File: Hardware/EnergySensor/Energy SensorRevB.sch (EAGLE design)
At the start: 42 parts, among them IC2 ATMega328p-pu, IC3 ld33v, Q1 16MHz, X1 MAINS IN

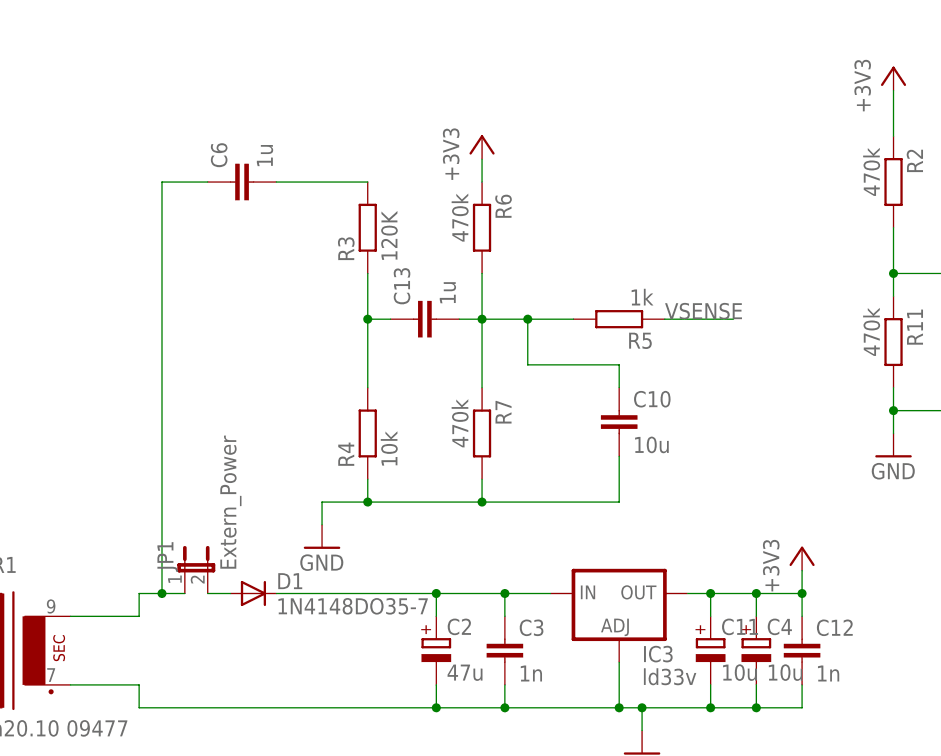
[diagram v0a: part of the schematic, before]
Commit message: FIXED MAJOR BUG  - schematic was incorrect for power measurements
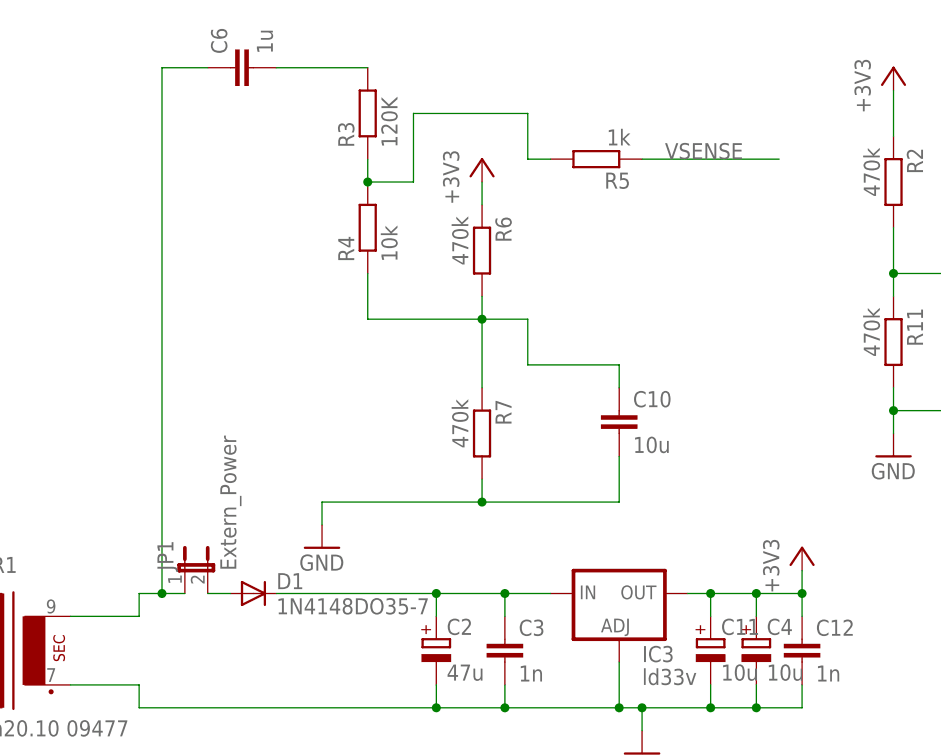
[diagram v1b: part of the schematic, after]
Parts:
- removed C13: 1u, rcl:C-EUC1206K
- R4: device rcl:R-EU_0207/7 -> rcl:R-EU_R1206
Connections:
- removed net N$10: C10.1, C13.2, R5.2, R6.2, R7.1
- new net N$11: C10.1, R4.1, R6.2, R7.1
- net GND: no longer R4.1
- net N$9: now also R5.2; no longer C13.1
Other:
- moved on the sheet: C6, R3, R4, R5, R6
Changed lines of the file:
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@@
 <part name="C6" library="rcl" deviceset="C-EU" device="C1206K" value="1u"/>
 <part name="R3" library="rcl" deviceset="R-EU_" device="0207/7" value="120K"/>
-<part name="R4" library="rcl" deviceset="R-EU_" device="0207/7" value="10k"/>
+<part name="R4" library="rcl" deviceset="R-EU_" device="R1206" value="10k"/>
 <part name="R5" library="rcl" deviceset="R-EU_" device="0207/7" value="1k"/>
 <part name="R6" library="rcl" deviceset="R-EU_" device="0207/7" value="470k"/>
@@
 <part name="GND9" library="supply1" deviceset="GND" device=""/>
 <part name="+3V6" library="supply1" deviceset="+3V3" device=""/>
-<part name="C13" library="rcl" deviceset="C-EU" device="C1206K" value="1u"/>
 <part name="JP1" library="jumper" deviceset="JP1E" device="" value="Extern_Power"/>
 <part name="H1" library="holes" deviceset="MOUNT-HOLE" device="2.8"/>
@@
 <instance part="C3" gate="G$1" x="101.6" y="78.74"/>
 <instance part="GND1" gate="1" x="116.84" y="66.04"/>
-<instance part="C6" gate="G$1" x="71.12" y="129.54" rot="R90"/>
-<instance part="R3" gate="G$1" x="86.36" y="124.46" rot="R90"/>
-<instance part="R4" gate="G$1" x="86.36" y="101.6" rot="R90"/>
-<instance part="R5" gate="G$1" x="114.3" y="114.3" rot="R180"/>
-<instance part="R6" gate="G$1" x="99.06" y="124.46" rot="R270"/>
+<instance part="C6" gate="G$1" x="71.12" y="142.24" rot="R90"/>
+<instance part="R3" gate="G$1" x="86.36" y="137.16" rot="R90"/>
+<instance part="R4" gate="G$1" x="86.36" y="124.46" rot="R90"/>
+<instance part="R5" gate="G$1" x="111.76" y="132.08" rot="R180"/>
+<instance part="R6" gate="G$1" x="99.06" y="121.92" rot="R270"/>
 <instance part="R7" gate="G$1" x="99.06" y="101.6" rot="R270"/>
 <instance part="GND3" gate="1" x="81.28" y="88.9"/>
@@
 <instance part="R10" gate="G$1" x="175.26" y="48.26" rot="R90"/>
 <instance part="GND9" gate="1" x="180.34" y="25.4"/>
-<instance part="+3V6" gate="G$1" x="99.06" y="134.62"/>
-<instance part="C13" gate="G$1" x="91.44" y="114.3" rot="R90"/>
+<instance part="+3V6" gate="G$1" x="99.06" y="132.08"/>
 <instance part="JP1" gate="A" x="66.04" y="86.36"/>
 <instance part="H1" gate="G$1" x="241.3" y="40.64"/>
@@
 <wire x1="60.96" y1="83.82" x2="63.5" y2="83.82" width="0.1524" layer="91"/>
 <pinref part="C6" gate="G$1" pin="1"/>
-<wire x1="63.5" y1="83.82" x2="63.5" y2="129.54" width="0.1524" layer="91"/>
-<wire x1="63.5" y1="129.54" x2="68.58" y2="129.54" width="0.1524" layer="91"/>
+<wire x1="63.5" y1="83.82" x2="63.5" y2="142.24" width="0.1524" layer="91"/>
+<wire x1="63.5" y1="142.24" x2="68.58" y2="142.24" width="0.1524" layer="91"/>
 <pinref part="TR1" gate="1" pin="S4"/>
 <wire x1="60.96" y1="81.28" x2="53.34" y2="81.28" width="0.1524" layer="91"/>
@@
 <pinref part="R7" gate="G$1" pin="2"/>
 <wire x1="99.06" y1="96.52" x2="99.06" y2="93.98" width="0.1524" layer="91"/>
-<wire x1="99.06" y1="93.98" x2="86.36" y2="93.98" width="0.1524" layer="91"/>
+<wire x1="99.06" y1="93.98" x2="81.28" y2="93.98" width="0.1524" layer="91"/>
 <pinref part="GND3" gate="1" pin="GND"/>
-<wire x1="86.36" y1="93.98" x2="81.28" y2="93.98" width="0.1524" layer="91"/>
 <wire x1="81.28" y1="93.98" x2="81.28" y2="91.44" width="0.1524" layer="91"/>
 <pinref part="C10" gate="G$1" pin="2"/>
@@
 <wire x1="114.3" y1="93.98" x2="99.06" y2="93.98" width="0.1524" layer="91"/>
 <junction x="99.06" y="93.98"/>
-<pinref part="R4" gate="G$1" pin="1"/>
-<wire x1="86.36" y1="96.52" x2="86.36" y2="93.98" width="0.1524" layer="91"/>
-<junction x="86.36" y="93.98"/>
 </segment>
 <segment>
@@
 <pinref part="C6" gate="G$1" pin="2"/>
 <pinref part="R3" gate="G$1" pin="2"/>
-<wire x1="76.2" y1="129.54" x2="86.36" y2="129.54" width="0.1524" layer="91"/>
+<wire x1="76.2" y1="142.24" x2="86.36" y2="142.24" width="0.1524" layer="91"/>
 </segment>
 </net>
@@
 <pinref part="R3" gate="G$1" pin="1"/>
 <pinref part="R4" gate="G$1" pin="2"/>
-<wire x1="86.36" y1="119.38" x2="86.36" y2="114.3" width="0.1524" layer="91"/>
-<junction x="86.36" y="114.3"/>
-<wire x1="86.36" y1="114.3" x2="86.36" y2="106.68" width="0.1524" layer="91"/>
-<pinref part="C13" gate="G$1" pin="1"/>
-<wire x1="88.9" y1="114.3" x2="86.36" y2="114.3" width="0.1524" layer="91"/>
+<wire x1="86.36" y1="132.08" x2="86.36" y2="129.54" width="0.1524" layer="91"/>
+<pinref part="R5" gate="G$1" pin="2"/>
+<wire x1="106.68" y1="132.08" x2="104.14" y2="132.08" width="0.1524" layer="91"/>
+<wire x1="104.14" y1="132.08" x2="104.14" y2="137.16" width="0.1524" layer="91"/>
+<wire x1="104.14" y1="137.16" x2="91.44" y2="137.16" width="0.1524" layer="91"/>
+<wire x1="91.44" y1="137.16" x2="91.44" y2="129.54" width="0.1524" layer="91"/>
+<wire x1="91.44" y1="129.54" x2="86.36" y2="129.54" width="0.1524" layer="91"/>
+<junction x="86.36" y="129.54"/>
 </segment>
 </net>
@@
 <segment>
 <pinref part="R5" gate="G$1" pin="1"/>
-<label x="119.38" y="114.3" size="1.778" layer="95"/>
-<wire x1="119.38" y1="114.3" x2="127" y2="114.3" width="0.1524" layer="91"/>
+<label x="119.38" y="132.08" size="1.778" layer="95"/>
+<wire x1="116.84" y1="132.08" x2="132.08" y2="132.08" width="0.1524" layer="91"/>
 </segment>
 <segment>
@@
 <segment>
 <pinref part="R6" gate="G$1" pin="1"/>
-<wire x1="99.06" y1="132.08" x2="99.06" y2="129.54" width="0.1524" layer="91"/>
+<wire x1="99.06" y1="129.54" x2="99.06" y2="127" width="0.1524" layer="91"/>
 <pinref part="+3V6" gate="G$1" pin="+3V3"/>
 </segment>
@@
 <pinref part="R10" gate="G$1" pin="2"/>
 <wire x1="175.26" y1="60.96" x2="175.26" y2="53.34" width="0.1524" layer="91"/>
-</segment>
-</net>
-<net name="N$10" class="0">
-<segment>
-<pinref part="R6" gate="G$1" pin="2"/>
-<pinref part="C13" gate="G$1" pin="2"/>
-<wire x1="99.06" y1="119.38" x2="99.06" y2="114.3" width="0.1524" layer="91"/>
-<wire x1="99.06" y1="114.3" x2="96.52" y2="114.3" width="0.1524" layer="91"/>
-<pinref part="R7" gate="G$1" pin="1"/>
-<wire x1="99.06" y1="106.68" x2="99.06" y2="114.3" width="0.1524" layer="91"/>
-<junction x="99.06" y="114.3"/>
-<pinref part="R5" gate="G$1" pin="2"/>
-<wire x1="109.22" y1="114.3" x2="104.14" y2="114.3" width="0.1524" layer="91"/>
-<pinref part="C10" gate="G$1" pin="1"/>
-<wire x1="104.14" y1="114.3" x2="99.06" y2="114.3" width="0.1524" layer="91"/>
-<wire x1="114.3" y1="106.68" x2="114.3" y2="109.22" width="0.1524" layer="91"/>
-<wire x1="114.3" y1="109.22" x2="104.14" y2="109.22" width="0.1524" layer="91"/>
-<wire x1="104.14" y1="109.22" x2="104.14" y2="114.3" width="0.1524" layer="91"/>
-<junction x="104.14" y="114.3"/>
 </segment>
 </net>
@@
 </segment>
 </net>
+<net name="N$11" class="0">
+<segment>
+<pinref part="R4" gate="G$1" pin="1"/>
+<wire x1="86.36" y1="119.38" x2="86.36" y2="114.3" width="0.1524" layer="91"/>
+<pinref part="R6" gate="G$1" pin="2"/>
+<wire x1="99.06" y1="116.84" x2="99.06" y2="114.3" width="0.1524" layer="91"/>
+<pinref part="R7" gate="G$1" pin="1"/>
+<wire x1="99.06" y1="106.68" x2="99.06" y2="114.3" width="0.1524" layer="91"/>
+<junction x="99.06" y="114.3"/>
+<pinref part="C10" gate="G$1" pin="1"/>
+<wire x1="104.14" y1="114.3" x2="99.06" y2="114.3" width="0.1524" layer="91"/>
+<wire x1="114.3" y1="106.68" x2="114.3" y2="109.22" width="0.1524" layer="91"/>
+<wire x1="114.3" y1="109.22" x2="104.14" y2="109.22" width="0.1524" layer="91"/>
+<wire x1="104.14" y1="109.22" x2="104.14" y2="114.3" width="0.1524" layer="91"/>
+<wire x1="86.36" y1="114.3" x2="99.06" y2="114.3" width="0.1524" layer="91"/>
+</segment>
+</net>

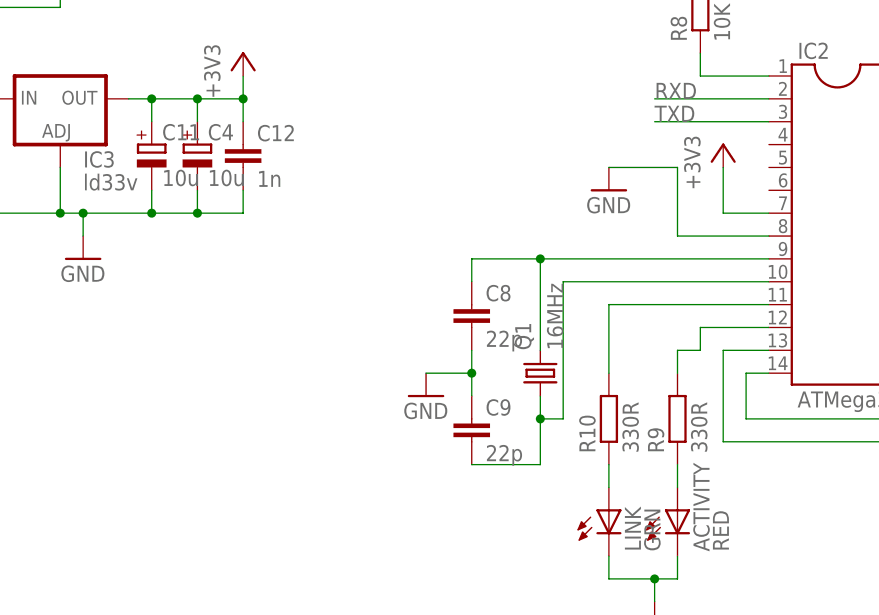
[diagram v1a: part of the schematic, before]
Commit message: updated BOM with finalised pricelist
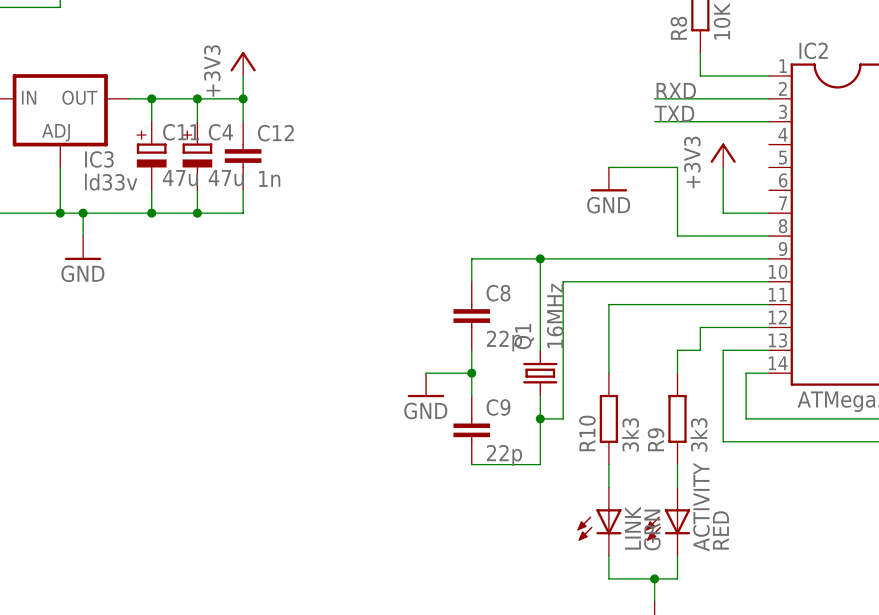
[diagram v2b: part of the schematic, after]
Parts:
- C11, C4: value 10u -> 47u
- R10, R9: value 330R -> 3k3
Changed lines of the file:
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@@
 <part name="+3V4" library="supply1" deviceset="+3V3" device=""/>
 <part name="+3V5" library="supply1" deviceset="+3V3" device=""/>
-<part name="C11" library="rcl" deviceset="CPOL-EU" device="E3.5-8" value="10u"/>
+<part name="C11" library="rcl" deviceset="CPOL-EU" device="E3.5-8" value="47u"/>
 <part name="C12" library="rcl" deviceset="C-EU" device="025-025X050" value="1n"/>
 <part name="LINK" library="led" deviceset="LED" device="5MM" value="GRN"/>
 <part name="ACTIVITY" library="led" deviceset="LED" device="5MM" value="RED"/>
-<part name="R9" library="rcl" deviceset="R-EU_" device="0207/7" value="330R"/>
-<part name="R10" library="rcl" deviceset="R-EU_" device="0207/7" value="330R"/>
+<part name="R9" library="rcl" deviceset="R-EU_" device="0207/7" value="3k3"/>
+<part name="R10" library="rcl" deviceset="R-EU_" device="0207/7" value="3k3"/>
 <part name="GND9" library="supply1" deviceset="GND" device=""/>
 <part name="+3V6" library="supply1" deviceset="+3V3" device=""/>
@@
 <part name="U$1" library="jack" deviceset="3.5MMJACK" device=""/>
 <part name="R13" library="rcl" deviceset="R-EU_" device="0207/7" value="1k"/>
-<part name="C4" library="rcl" deviceset="CPOL-EU" device="E3.5-8" value="10u"/>
+<part name="C4" library="rcl" deviceset="CPOL-EU" device="E3.5-8" value="47u"/>
 <part name="C5" library="rcl" deviceset="C-EU" device="C1206K" value="100n"/>
 <part name="L1" library="rcl" deviceset="L-EU" device="L3230M" value="10u"/>
